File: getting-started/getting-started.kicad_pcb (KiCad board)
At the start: 2 copper layers, 0 parts

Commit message: Import from schematic
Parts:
- added BT1: 3V, Battery:BatteryHolder_Keystone_1058_1x2032, F.Cu at (140.3, 104.1)
- added D1: red, LED_THT:LED_D5.0mm, F.Cu at (141.6, 120.2)
- added R1: 1k, Resistor_THT:R_Axial_DIN0309_L9.0mm_D3.2mm_P12.70mm_Horizontal, F.Cu at (124.9, 118.8)

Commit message: Edge.Cuts
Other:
- board outline added: 38.1 x 38.1 mm
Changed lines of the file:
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@@
     )
   )
+  (gr_rect (start 121.92 88.9) (end 160.02 127)
+    (stroke (width 0.1) (type default)) (fill none) (layer "Edge.Cuts"))
 )

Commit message: Routing tracks
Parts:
- BT1: moved to B.Cu
- moved R1 30.1 mm to (154.7, 123.0), turned to 180 degrees
- moved D1 16.3 mm to (125.3, 120.4), turned to -90 degrees
- moved BT1 1.25 mm to (140.0, 105.4), turned to 180 degrees
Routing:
- net VCC: track 0.00 -> 17.9 mm, vias 0 -> 1
- net /led: track 0.00 -> 16.7 mm
- net GND: track 0.00 -> 15.1 mm
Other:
- board size 38.1 x 38.1 mm -> 40 x 40 mm

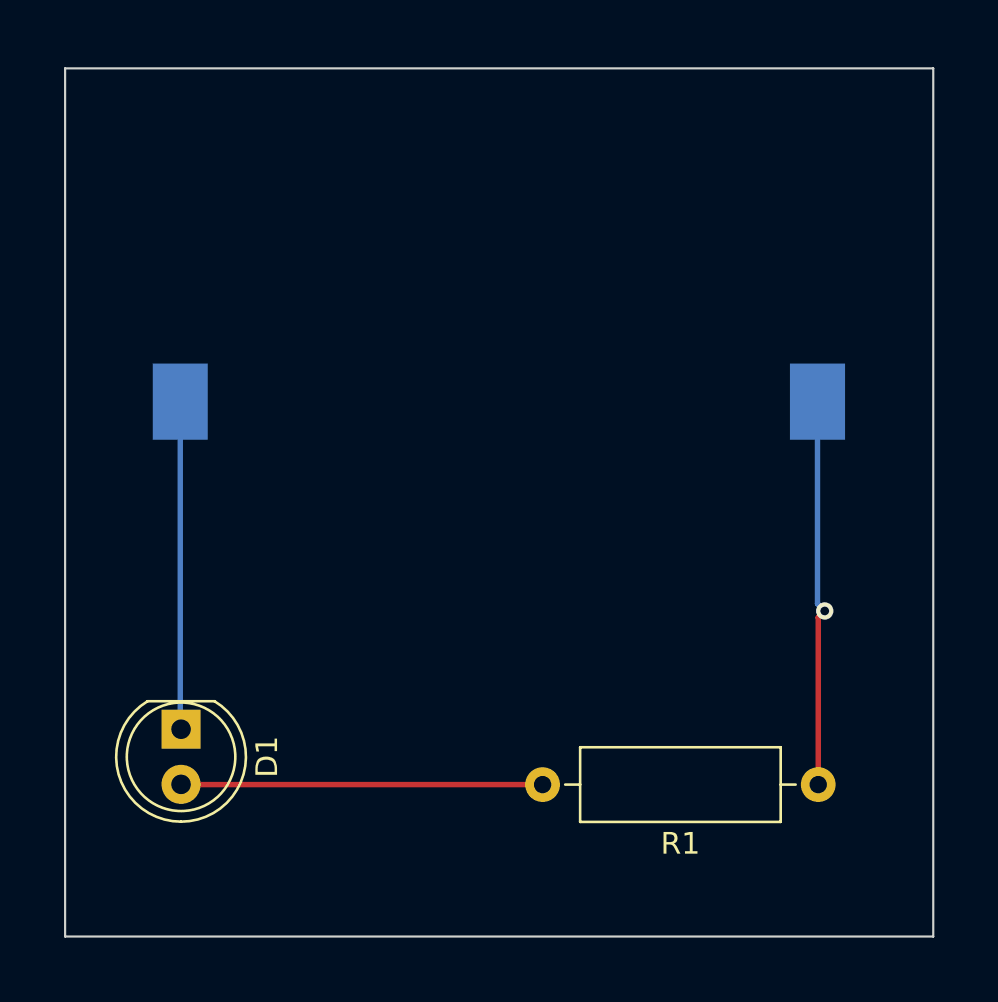
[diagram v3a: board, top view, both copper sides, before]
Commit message: Copper zone for ground
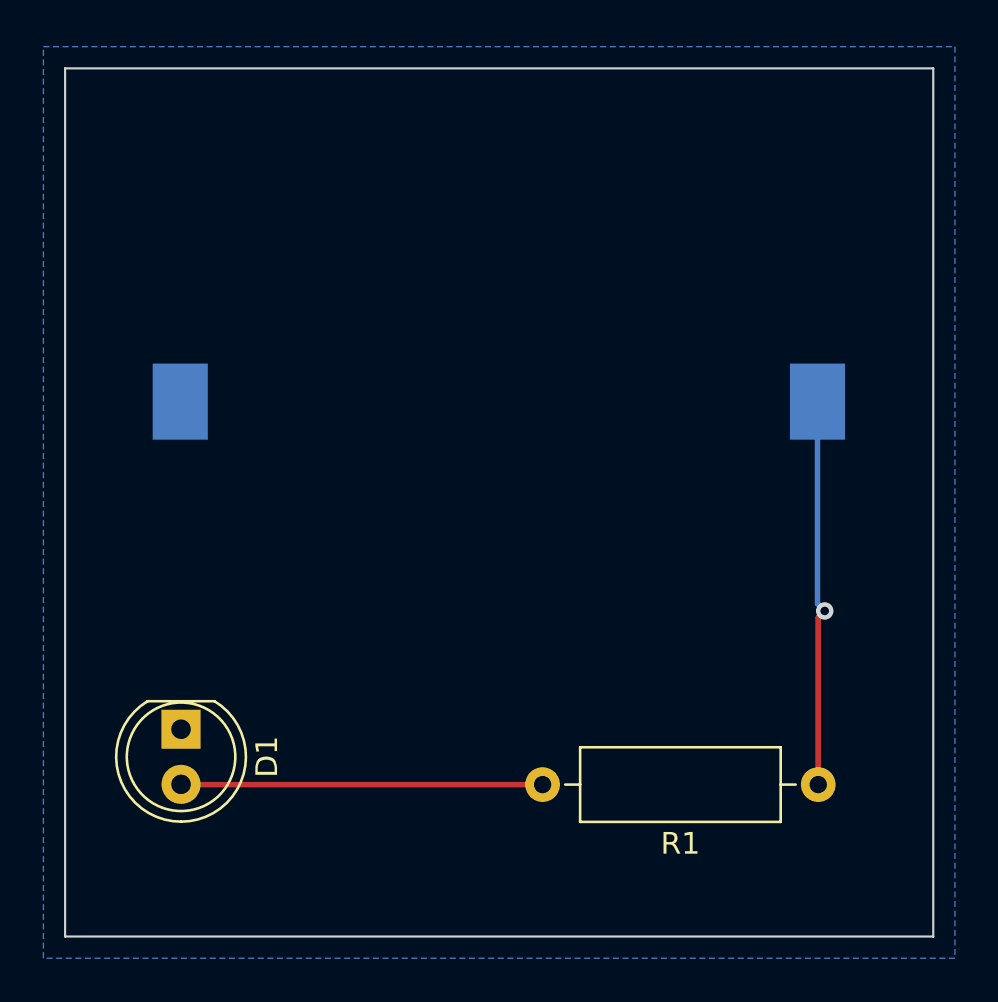
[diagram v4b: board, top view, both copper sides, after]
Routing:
- net GND: track 15.1 -> 0.05 mm
- added copper zone on B.Cu, net GND
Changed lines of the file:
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@@
   (segment (start 154.665891 114.665891) (end 155 115) (width 0.25) (layer "B.Cu") (net 1))
   (segment (start 154.665891 105.355936) (end 154.665891 114.665891) (width 0.25) (layer "B.Cu") (net 1))
-  (segment (start 125.305891 105.355936) (end 125.305891 120.412861) (width 0.25) (layer "B.Cu") (net 2))
   (segment (start 125.305891 120.412861) (end 125.342173 120.449143) (width 0.25) (layer "B.Cu") (net 2))
   (segment (start 125.35303 123) (end 125.342173 122.989143) (width 0.25) (layer "F.Cu") (net 3))
   (segment (start 142 123) (end 125.35303 123) (width 0.25) (layer "F.Cu") (net 3))
+  (zone (net 2) (net_name "GND") (layer "B.Cu") (hatch edge 0.5)
+    (connect_pads (clearance 0.5))
+    (min_thickness 0.25) (filled_areas_thickness no)
+    (fill yes (thermal_gap 0.5) (thermal_bridge_width 0.5))
+    (polygon
+      (pts
+        (xy 119 89)
+        (xy 161 89)
+        (xy 161 131)
+        (xy 119 131)
+      )
+    )
+  )
 )
